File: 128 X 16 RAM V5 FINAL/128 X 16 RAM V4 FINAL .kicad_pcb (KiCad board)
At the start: 4 copper layers, 180 x 95 mm, 112 parts, among them J1 DIP16 Socket, J11 +5V IN, J2 RUN/RST, J3 DB25_Pins, J4 SR REGISTER, J5 Input, J6 LA/DEP, J7 Output, U1 D2115, U10 D2115, U11 D2115, U12 D2115, U13 D2115, U14 D2115, U15 D2115, U16 D2115, U18 74LS138, U19 4017, U2 D2115, U20 74LS138, U21 74LS07, U22 74LS157, U23 74LS541, U24 74LS04, U25 74LS123, U26 74LS00, U27 74LS595, U3 D2115, U4 D2115, U5 D2115, U6 D2115, U7 D2115, U8 D2115, U9 D2115

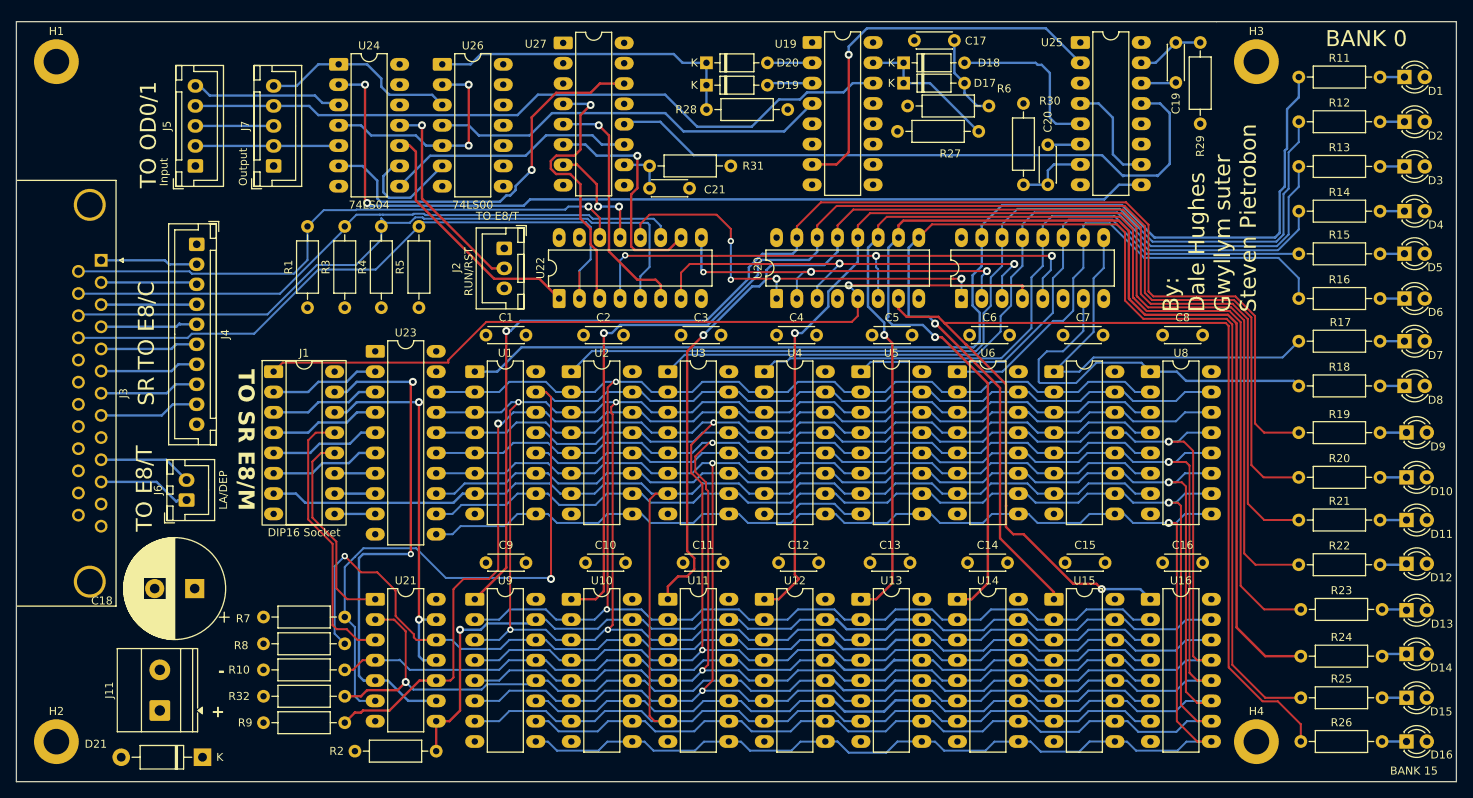
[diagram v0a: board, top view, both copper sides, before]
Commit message: 128x16 RAM V5 update
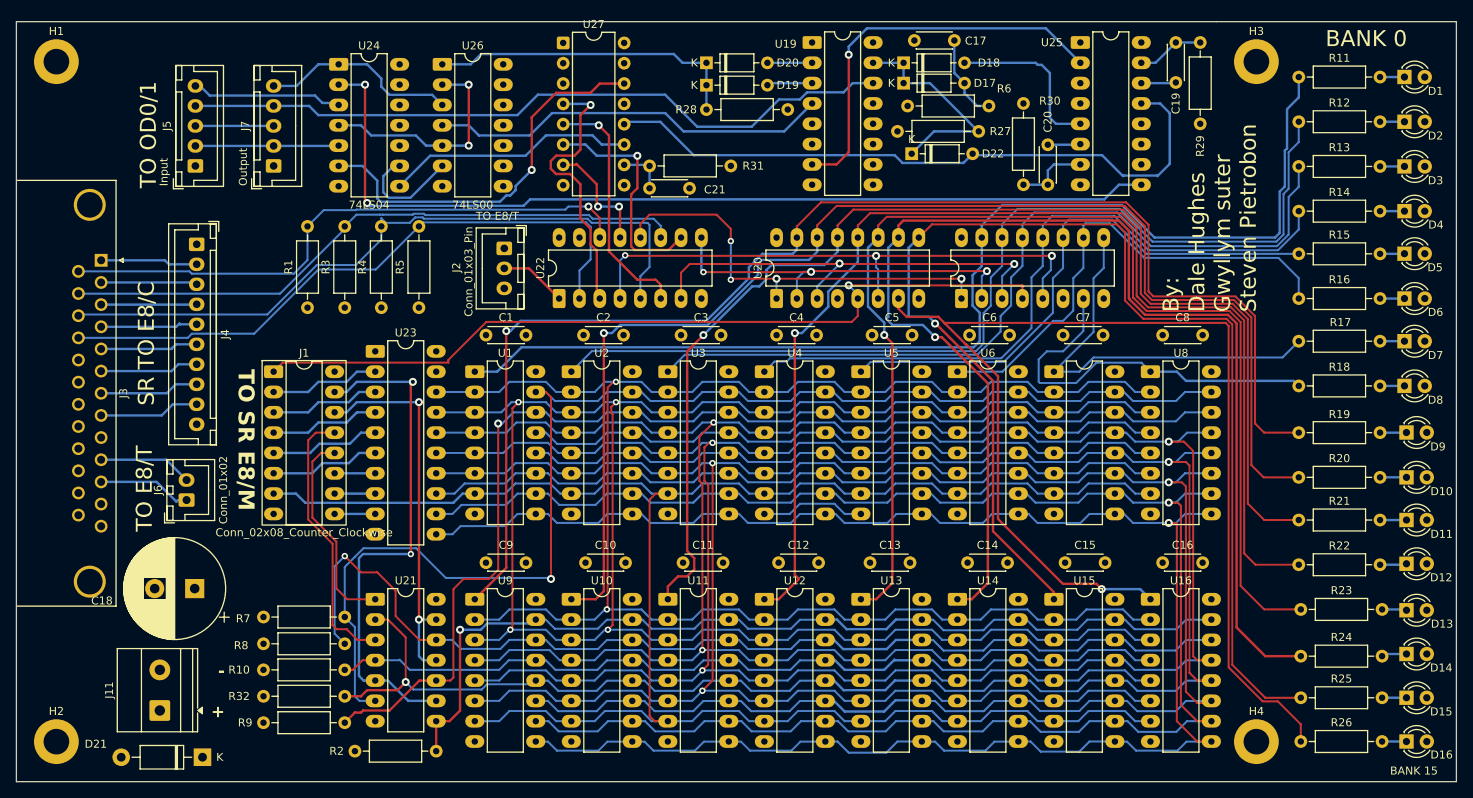
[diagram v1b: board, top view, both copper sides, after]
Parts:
- added D22: BAT48, Diode_THT:D_DO-35_SOD27_P7.62mm_Horizontal, F.Cu at (176.9, 71.5)
- C19, C20: value 220pF -> 1nF
- H1, H2, H3, H4: value M3 -> MountingHole_Pad
- J1: value DIP16 Socket -> Conn_02x08_Counter_Clockwise
- J11: value +5V IN -> Conn_01x02
- J2: value RUN/RST -> Conn_01x03_Pin
- J4: value SR REGISTER -> Conn_01x10
- J6: value LA/DEP -> Conn_01x02
- U27: footprint Package_DIP:DIP-16_W7.62mm_LongPads -> Package_DIP:DIP-16_W7.62mm
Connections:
- J2 pad 2: ~{RUN} -> ~{DEP+LA}
- U22 pad 1: Net-(U22-S) -> ~{DEP+LA}
- U24 pad 10: Net-(U22-S) -> (no net)
- U24 pad 11: ~{RUN} -> (no net)
- U25 pad 10: Net-(U25A-~{Q}) -> +5V
- U25 pad 4: Net-(U25A-~{Q}) -> unconnected-(U25A-~{Q}-Pad4)
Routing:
- net Net-(U22-S): track 31.4 -> 0.00 mm
- net ~{RUN}: track 25.8 -> 0.00 mm, vias 1 -> 0
- net Net-(U25A-~{Q}): track 13.5 -> 0.00 mm
- net Net-(D17-K): track 18.2 -> 27.8 mm
- net ~{DEP+LA}: track 0.00 -> 8.42 mm
- net 8: track 83.1 -> 79.8 mm
- net /Latch Bank: track 82.2 -> 83.2 mm
- net /A3: track 219.0 -> 218.1 mm
- net /A2: track 218.6 -> 217.8 mm
